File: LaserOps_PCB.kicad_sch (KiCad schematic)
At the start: 22 parts, among them J1 Conn_01x02_Pin, J2 Status_leds, J3 Dome, Q1 NPN, Q2 NPN, Q3 NPN, Q4 NPN, SW1 SW_Push_DPDT, SW2 SW_Push, SW3 SW_Push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

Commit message: late night schmeatic with gotzi
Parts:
- removed BT1: 6V, symbol Device:Battery
- removed C1, C2: 10µF, symbol Device:C
- removed F1: Fuse, symbol Device:Fuse
- removed J1: Conn_01x02_Pin, symbol Connector:Conn_01x02_Pin
- removed J2: Status_leds, symbol Connector_Generic:Conn_01x04
- removed J3: Dome, symbol Connector_Generic:Conn_01x06
- removed Q1, Q2, Q3, Q4: NPN, symbol Simulation_SPICE:NPN
- removed R1: 10, symbol Device:R
- removed R2: 4k7, symbol Device:R
- removed R3: R_Variable, symbol Device:R_Variable
- removed R4: 10k, symbol Device:R
- removed R5, R7: 3k3, symbol Device:R
- removed R6: 2k2, symbol Device:R
- removed SW1: SW_Push_DPDT, symbol Switch:SW_Push_DPDT
- removed SW2, SW3: SW_Push, symbol Switch:SW_Push
- removed U1: AMS1117-3.3, Package_TO_SOT_SMD:SOT-223-3_TabPin2, symbol Regulator_Linear:AMS1117-3.3
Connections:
- no-connect marks 1 -> 0
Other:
- added sheet In_Out_puts (in_out_puts.kicad_sch)
- added sheet Power (power.kicad_sch)
- added sheet µC (µC.kicad_sch)
- note removed: "IR-Transmission"
- note removed: "Inputs"
- note removed: "Output"
- note removed: "Power"
- company: (none) -> made by Nico Hütter
- title: (none) -> Nerf-ATG

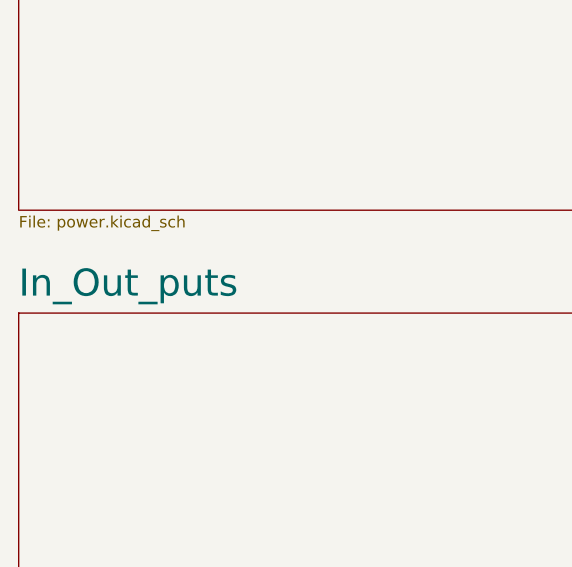
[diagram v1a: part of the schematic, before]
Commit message: simulated IR-constant-current circuit, worked on schematic
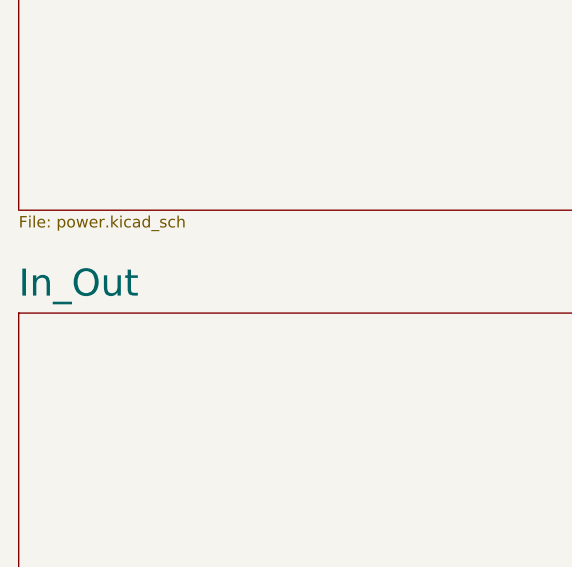
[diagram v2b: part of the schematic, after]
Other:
- sheet In_Out_puts renamed In_Out
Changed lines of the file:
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@@
 			(color 0 0 0 0.0000)
 		)
-		(property "Sheetname" "In_Out_puts"
+		(property "Sheetname" "In_Out"
 			(at 20.32 140.6634 0)
 			(effects

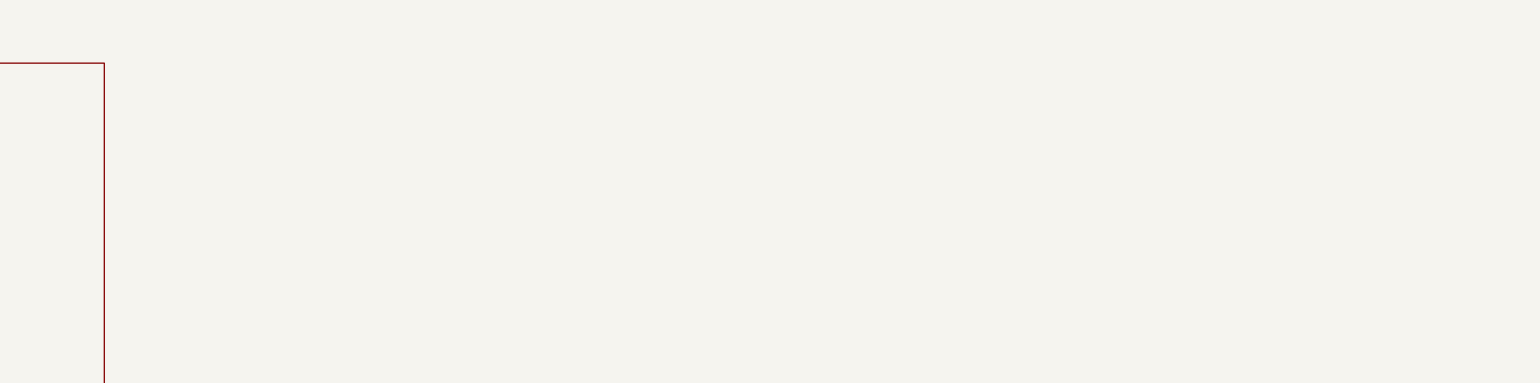
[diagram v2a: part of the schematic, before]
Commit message: prepared for jlcpcb ordering.
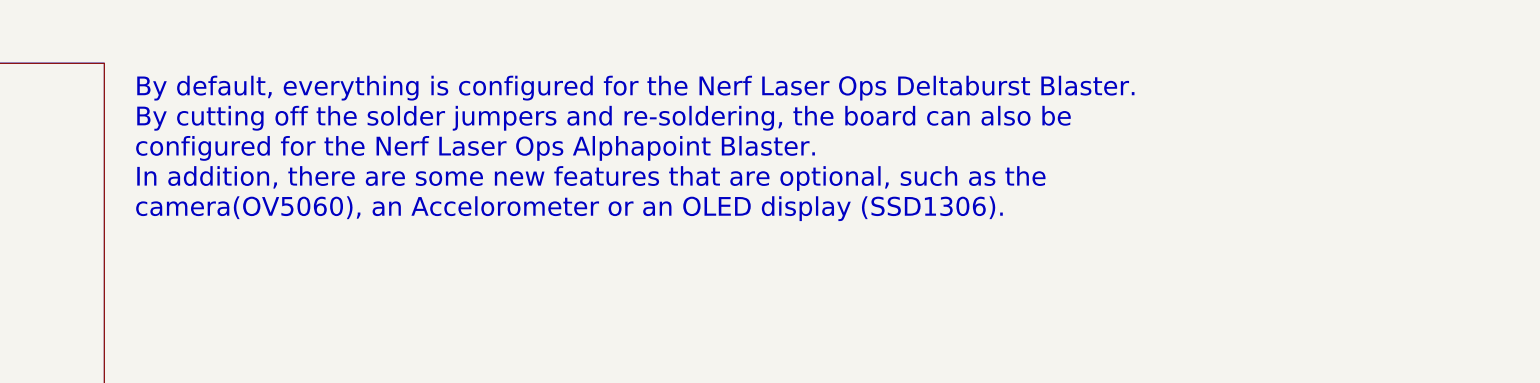
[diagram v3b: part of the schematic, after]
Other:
- note added: "By default, everything is configured for the Nerf Laser Ops Deltaburst Blaster. By cutting off the solder jumpers and re-soldering, the board can also be configured for the Nerf Laser Ops Alphapoint Blaster. In addition, there are some new features that are optional, such as the camera(OV5060), an Accelorometer or an OLED display (SSD1306)."
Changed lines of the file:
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@@
 		(company "made by Nico Hütter")
+	)
+	(text "By default, everything is configured for the Nerf Laser Ops Deltaburst Blaster.\nBy cutting off the solder jumpers and re-soldering, the board can also be\nconfigured for the Nerf Laser Ops Alphapoint Blaster.\nIn addition, there are some new features that are optional, such as the\ncamera(OV5060), an Accelorometer or an OLED display (SSD1306)."
+		(exclude_from_sim no)
+		(at 129.794 35.56 0)
+		(effects
+			(font
+				(size 2.5 2.5)
+			)
+			(justify left)
+		)
 	)
 	(sheet
